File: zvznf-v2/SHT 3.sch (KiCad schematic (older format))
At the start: 23 parts, among them IC1 PIC18F14K50, P2 CONN_01X06, P3 CONN_01X02, P4 CONN_01X04, SW7 SWITCH_INV, U1 M25P16, X1 USB_OTG, Y1 12 MHZ

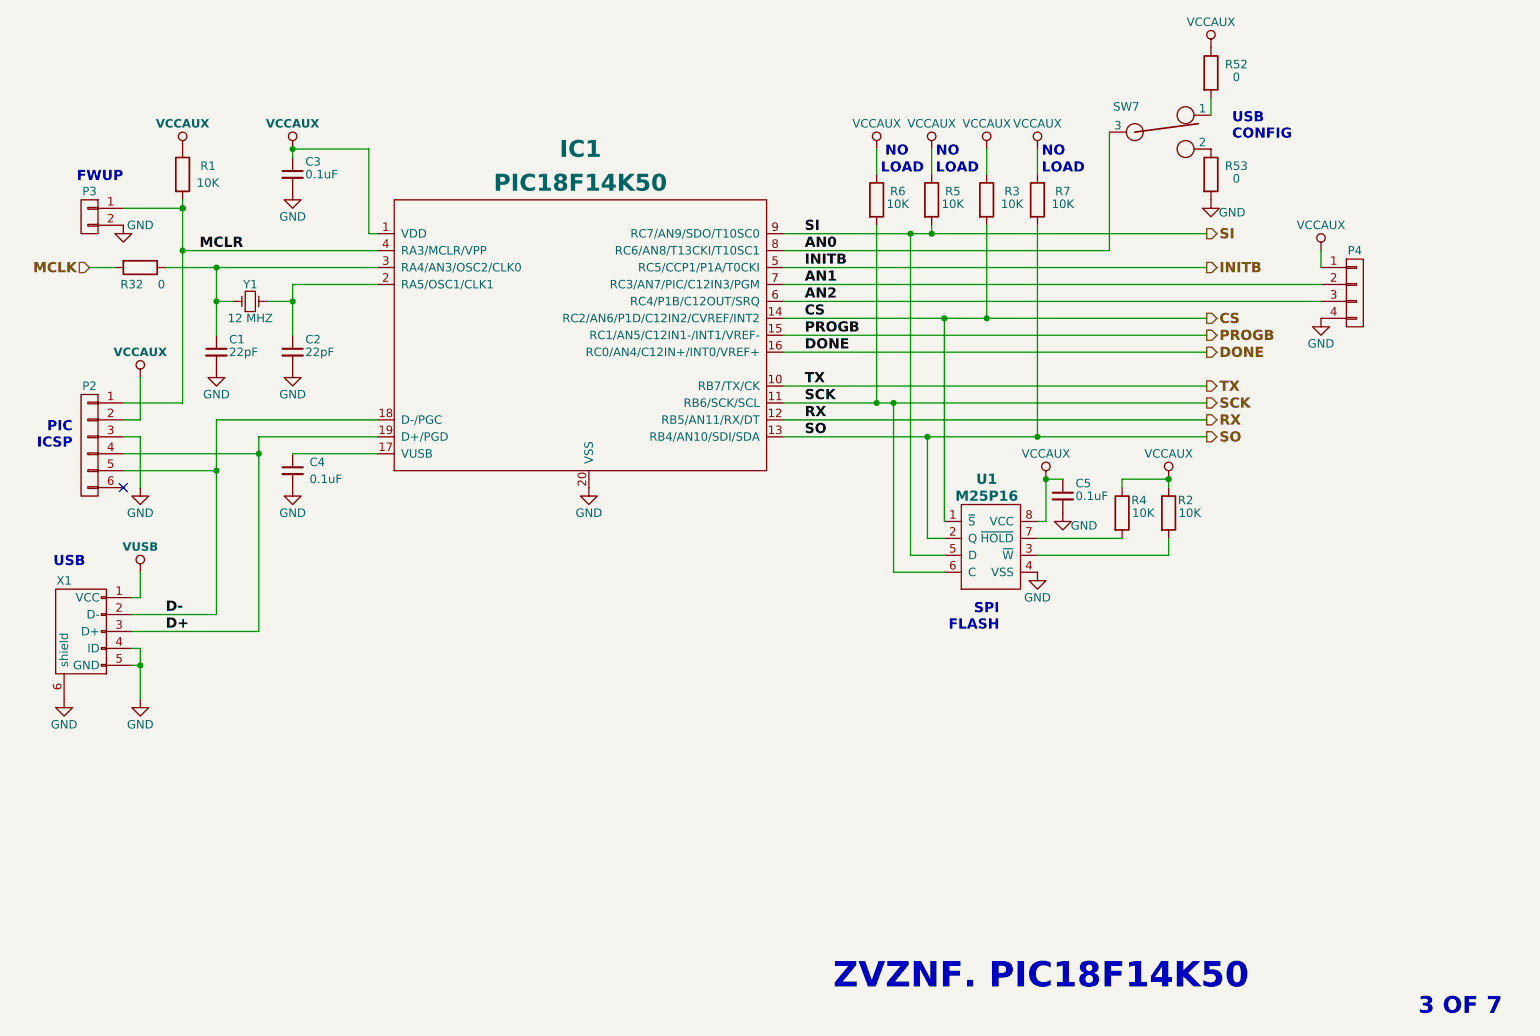
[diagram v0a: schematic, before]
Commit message: Fix USB connector on ZVZNF
Connector was rotated (pins unconnected, tracks going to nowhere), assuming footprint was changed at some point.
Assuming PIC18F14K50 is being used as USB slave, ID pin marked not-connected (pin not used if OTG is never used).
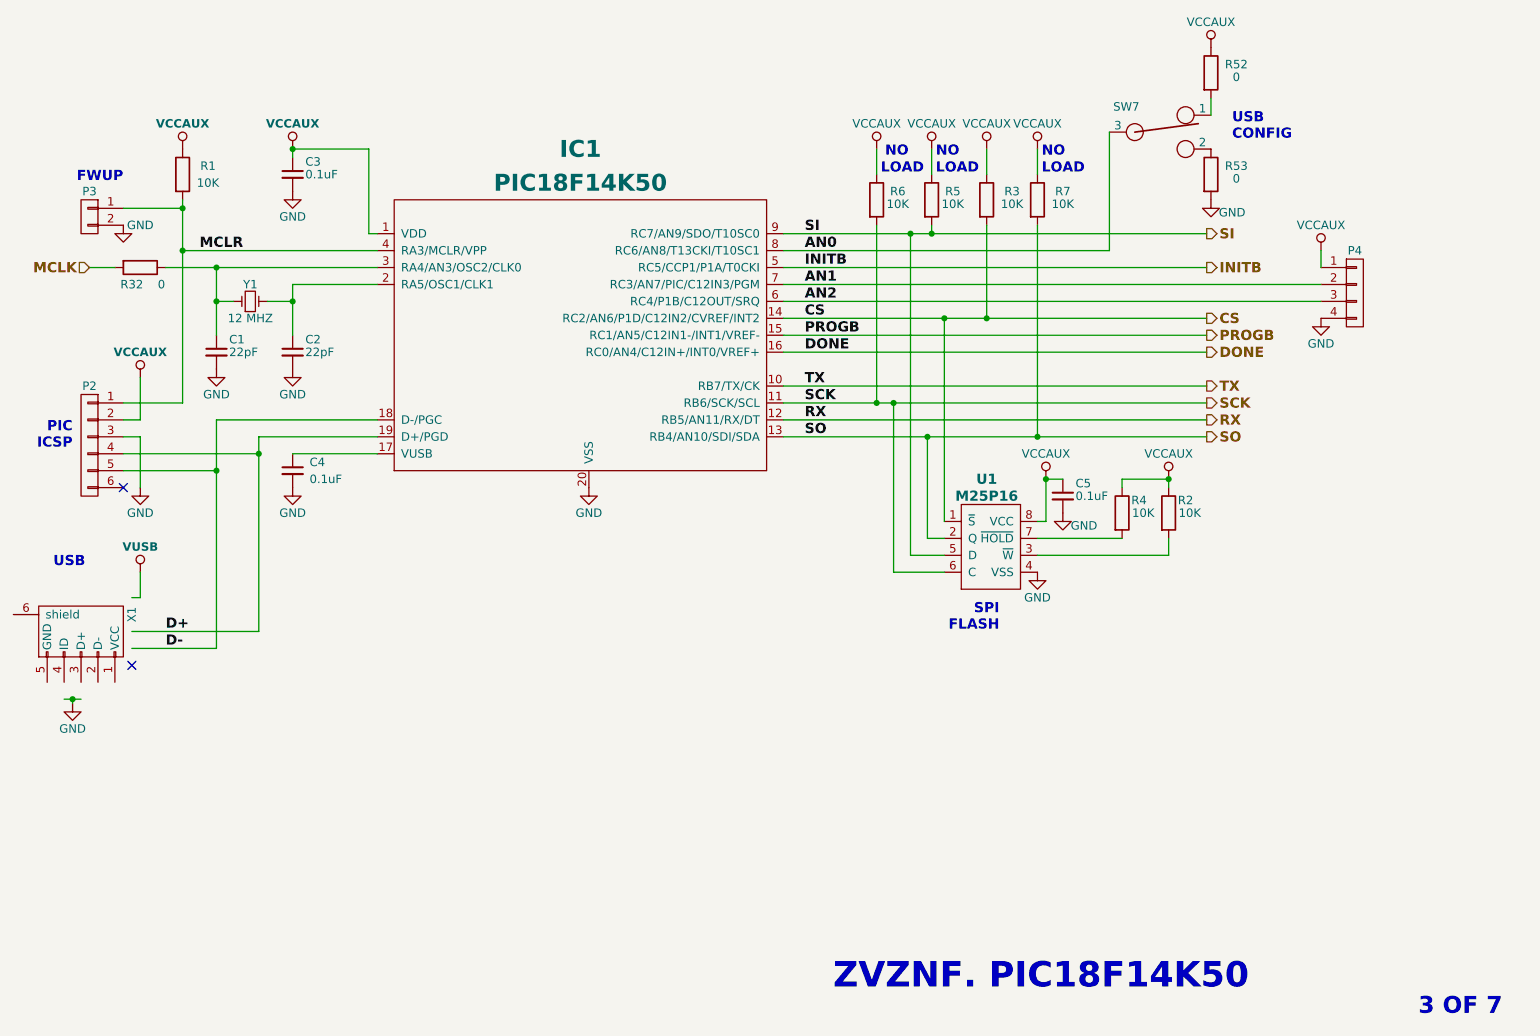
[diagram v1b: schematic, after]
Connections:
- wire segments 90 -> 72
- no-connect marks 1 -> 2
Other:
- moved on the sheet: X1
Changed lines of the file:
@@
 EESchema Schematic File Version 2
-LIBS:ZVZNF-cache
+LIBS:ZVZNF-rescue
 LIBS:power
 LIBS:device
@@
 LIBS:contrib
 LIBS:valves
+LIBS:ZVZNF-cache
 EELAYER 25 0
 EELAYER END
@@
 $EndComp
 Wire Wire Line
-	3250 2525 4350 2525
-Wire Wire Line
-	4350 2525 4400 2525
+	3250 2525 4400 2525
 Text Label 3350 2525 0    60   ~ 12
 MCLR
@@
 $EndComp
 Wire Wire Line
-	3150 2625 3450 2625
-Wire Wire Line
-	3450 2625 4400 2625
-Wire Wire Line
-	3450 2625 3450 2825
-Wire Wire Line
-	3450 2825 3450 3025
+	3150 2625 4400 2625
+Wire Wire Line
+	3450 2625 3450 3025
 Wire Wire Line
 	3450 2825 3550 2825
@@
 	4400 2725 3900 2725
 Wire Wire Line
-	3900 2725 3900 2825
-Wire Wire Line
-	3900 2825 3900 3025
+	3900 2725 3900 3025
 Wire Wire Line
 	3900 2825 3750 2825
@@
 	4400 3725 3900 3725
 Wire Wire Line
-	3700 3625 3700 3725
-Wire Wire Line
-	3700 3725 3700 4775
-Wire Wire Line
-	3450 3525 3450 3825
-Wire Wire Line
-	3450 3825 3450 4675
+	3700 3625 3700 4775
+Wire Wire Line
+	3450 4875 3450 3525
 $Comp
 L USB_OTG X1
 U 1 1 5A03A2B0
 P 2650 4775
+AR Path="/5A03A2B0" Ref="X1"  Part="1"
+AR Path="/5A037A9C/5A03A2B0" Ref="X1"  Part="1"
 F 0 "X1" V 2950 4875 50  0000 C CNN
 F 1 "USB_OTG" H 2650 4975 50  0001 C CNN
@@
 F 3 "" V 2600 4675 50  0000 C CNN
 	1    2650 4775
-	0    -1   -1   0
-$EndComp
-Wire Wire Line
-	3450 4675 2950 4675
+	1    0    0    -1
+$EndComp
 Wire Wire Line
 	3700 4775 2950 4775
@@
 	3450 3525 4400 3525
 Wire Wire Line
-	2900 3425 3250 3425
+	3250 3425 2900 3425
 Connection ~ 3250 2525
 $Comp
@@
 L GND #PWR?
 U 1 1 5A03BBFF
-P 2550 5175
-F 0 "#PWR?" H 2550 4925 50  0001 C CNN
-F 1 "GND" H 2550 5025 50  0000 C CNN
-F 2 "" H 2550 5175 50  0000 C CNN
-F 3 "" H 2550 5175 50  0000 C CNN
-	1    2550 5175
-	1    0    0    -1
-$EndComp
-Wire Wire Line
-	2950 4875 3000 4875
-Wire Wire Line
-	3000 4875 3000 4975
-Wire Wire Line
-	3000 4975 3000 5175
-Wire Wire Line
-	2950 4975 3000 4975
-Connection ~ 3000 4975
-$Comp
-L GND #PWR?
-U 1 1 5A03BCA9
-P 3000 5175
-F 0 "#PWR?" H 3000 4925 50  0001 C CNN
-F 1 "GND" H 3000 5025 50  0000 C CNN
-F 2 "" H 3000 5175 50  0000 C CNN
-F 3 "" H 3000 5175 50  0000 C CNN
-	1    3000 5175
-	1    0    0    -1
-$EndComp
+P 2600 5200
+F 0 "#PWR?" H 2600 4950 50  0001 C CNN
+F 1 "GND" H 2600 5050 50  0000 C CNN
+F 2 "" H 2600 5200 50  0000 C CNN
+F 3 "" H 2600 5200 50  0000 C CNN
+	1    2600 5200
+	1    0    0    -1
+$EndComp
+Wire Wire Line
+	2950 4875 3450 4875
 $Comp
 L CONN_01X02 P3
@@
 $EndComp
 Wire Wire Line
-	3250 2225 3250 2275
-Wire Wire Line
-	2900 2275 3250 2275
-Wire Wire Line
-	3250 2275 3250 2275
+	3250 2225 3250 3425
+Wire Wire Line
+	3250 2275 2900 2275
 $Comp
 L GND #PWR?
@@
 $EndComp
 Wire Wire Line
-	6800 2925 7750 2925
-Wire Wire Line
-	7750 2925 8000 2925
-Wire Wire Line
-	8000 2925 9300 2925
-Wire Wire Line
-	6800 3625 7650 3625
-Wire Wire Line
-	7650 3625 8300 3625
-Wire Wire Line
-	8300 3625 9300 3625
-Wire Wire Line
-	6800 3425 7350 3425
-Wire Wire Line
-	7350 3425 7450 3425
-Wire Wire Line
-	7450 3425 9300 3425
-Wire Wire Line
-	6800 2425 7550 2425
-Wire Wire Line
-	7550 2425 7675 2425
-Wire Wire Line
-	7675 2425 9300 2425
+	6800 2925 9300 2925
+Wire Wire Line
+	6800 3625 9300 3625
+Wire Wire Line
+	6800 3425 9300 3425
+Wire Wire Line
+	6800 2425 9300 2425
 $Comp
 L GND #PWR?
@@
 	1    0    0    -1
 $EndComp
-Wire Wire Line
-	3250 3425 3250 2275
-Connection ~ 3250 2275
-Text Label 3150 4675 0    60   ~ 12
+Text Label 3150 4875 0    60   ~ 12
 D-
 Text Label 3150 4775 0    60   ~ 12
@@
 Text Notes 8325 2075 0    60   ~ 12
 LOAD
+Wire Wire Line
+	2550 5175 2650 5175
+Wire Wire Line
+	2600 5175 2600 5200
+Connection ~ 2600 5175
+NoConn ~ 2950 4975
 $EndSCHEMATC
